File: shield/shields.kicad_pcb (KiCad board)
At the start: 2 copper layers, 40.4 x 95.7 mm, 1 part

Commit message: Update as ordered.
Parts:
- added REF**: C_1210_3225Metric_Pad1.33x2.70mm_HandSolder, Swadge_Parts:C_1210_3225Metric_Pad1.33x2.70mm_HandSolder, F.Cu at (28.7, 116.0)
- added REF**: C_1210_3225Metric_Pad1.33x2.70mm_HandSolder, Swadge_Parts:C_1210_3225Metric_Pad1.33x2.70mm_HandSolder, F.Cu at (23.5, 73.1)
- added REF**: C_1210_3225Metric_Pad1.33x2.70mm_HandSolder, Swadge_Parts:C_1210_3225Metric_Pad1.33x2.70mm_HandSolder, F.Cu at (50.2, 30.3)
- added REF**: C_1210_3225Metric_Pad1.33x2.70mm_HandSolder, Swadge_Parts:C_1210_3225Metric_Pad1.33x2.70mm_HandSolder, F.Cu at (54.9, 94.2)
- added REF**: C_1210_3225Metric_Pad1.33x2.70mm_HandSolder, Swadge_Parts:C_1210_3225Metric_Pad1.33x2.70mm_HandSolder, B.Cu at (55.0, 94.2)
- added REF**: C_1210_3225Metric_Pad1.33x2.70mm_HandSolder, Swadge_Parts:C_1210_3225Metric_Pad1.33x2.70mm_HandSolder, B.Cu at (29.1, 116.9)
- added REF**: C_1210_3225Metric_Pad1.33x2.70mm_HandSolder, Swadge_Parts:C_1210_3225Metric_Pad1.33x2.70mm_HandSolder, B.Cu at (50.2, 30.2)
- added REF**: C_1210_3225Metric_Pad1.33x2.70mm_HandSolder, Swadge_Parts:C_1210_3225Metric_Pad1.33x2.70mm_HandSolder, B.Cu at (23.5, 73.1)
- moved Ref** 114.5 mm to (86.2, 75.3)
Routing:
- net (no net): track 0.00 -> 5.20 mm
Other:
- rule pad_to_mask_clearance: 0.2 -> 0
- board text added: "Fab notes: 0.6mm Thick FR4"
- board text added: "Kidney Test Rev A"

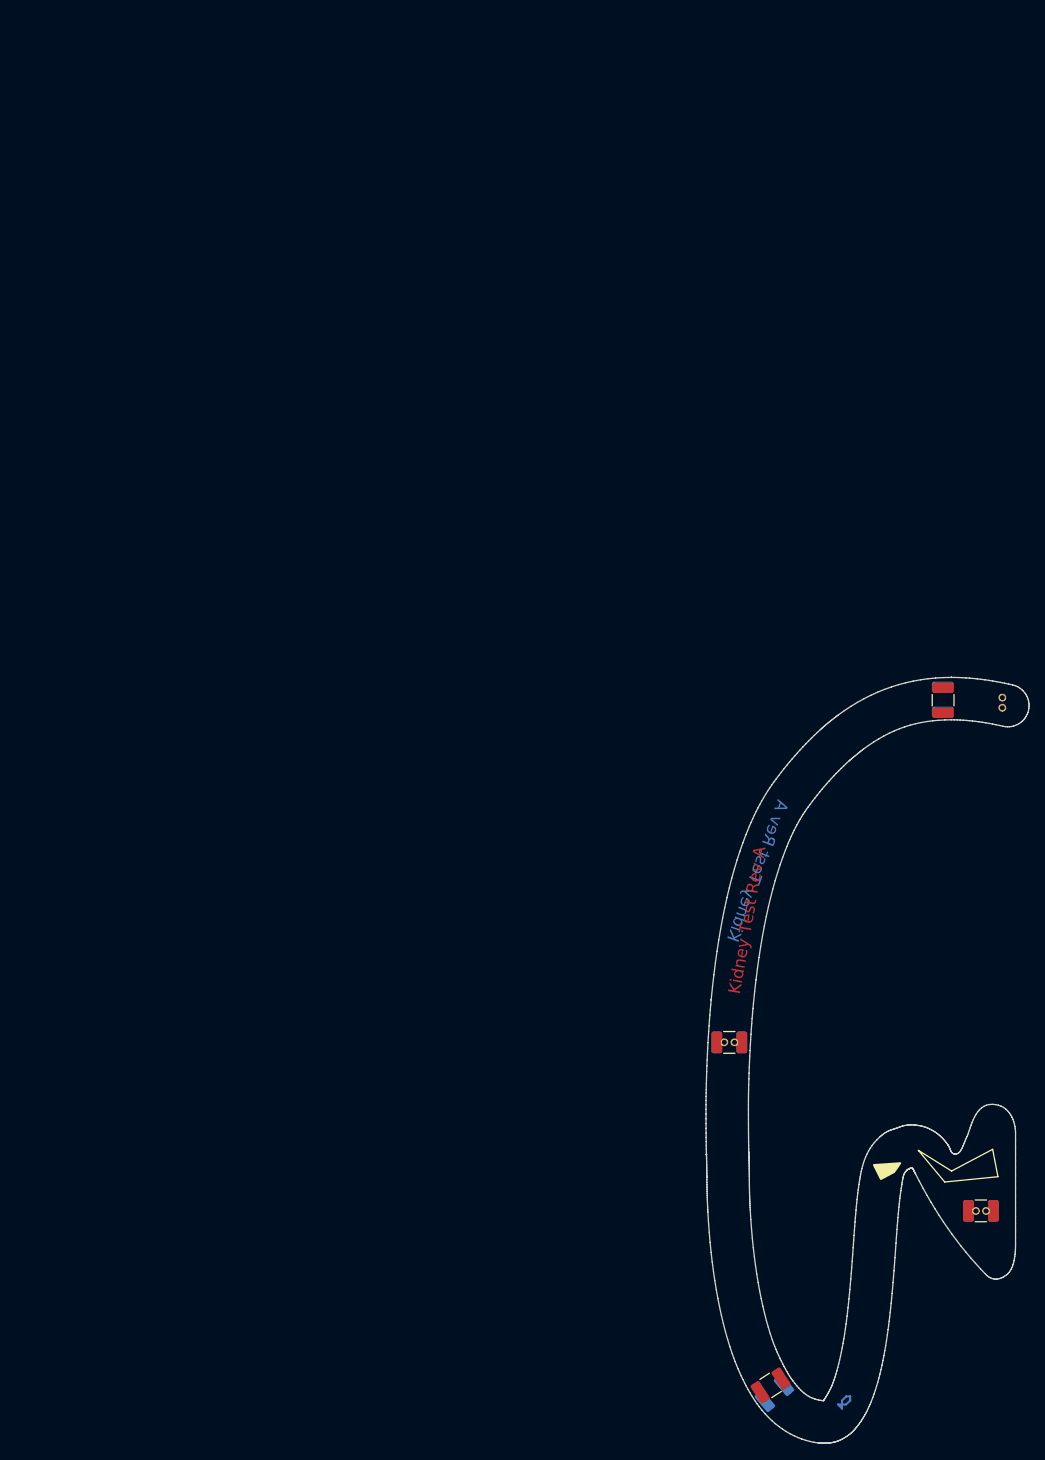
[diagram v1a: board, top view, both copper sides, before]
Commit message: Put squarewave art on shields
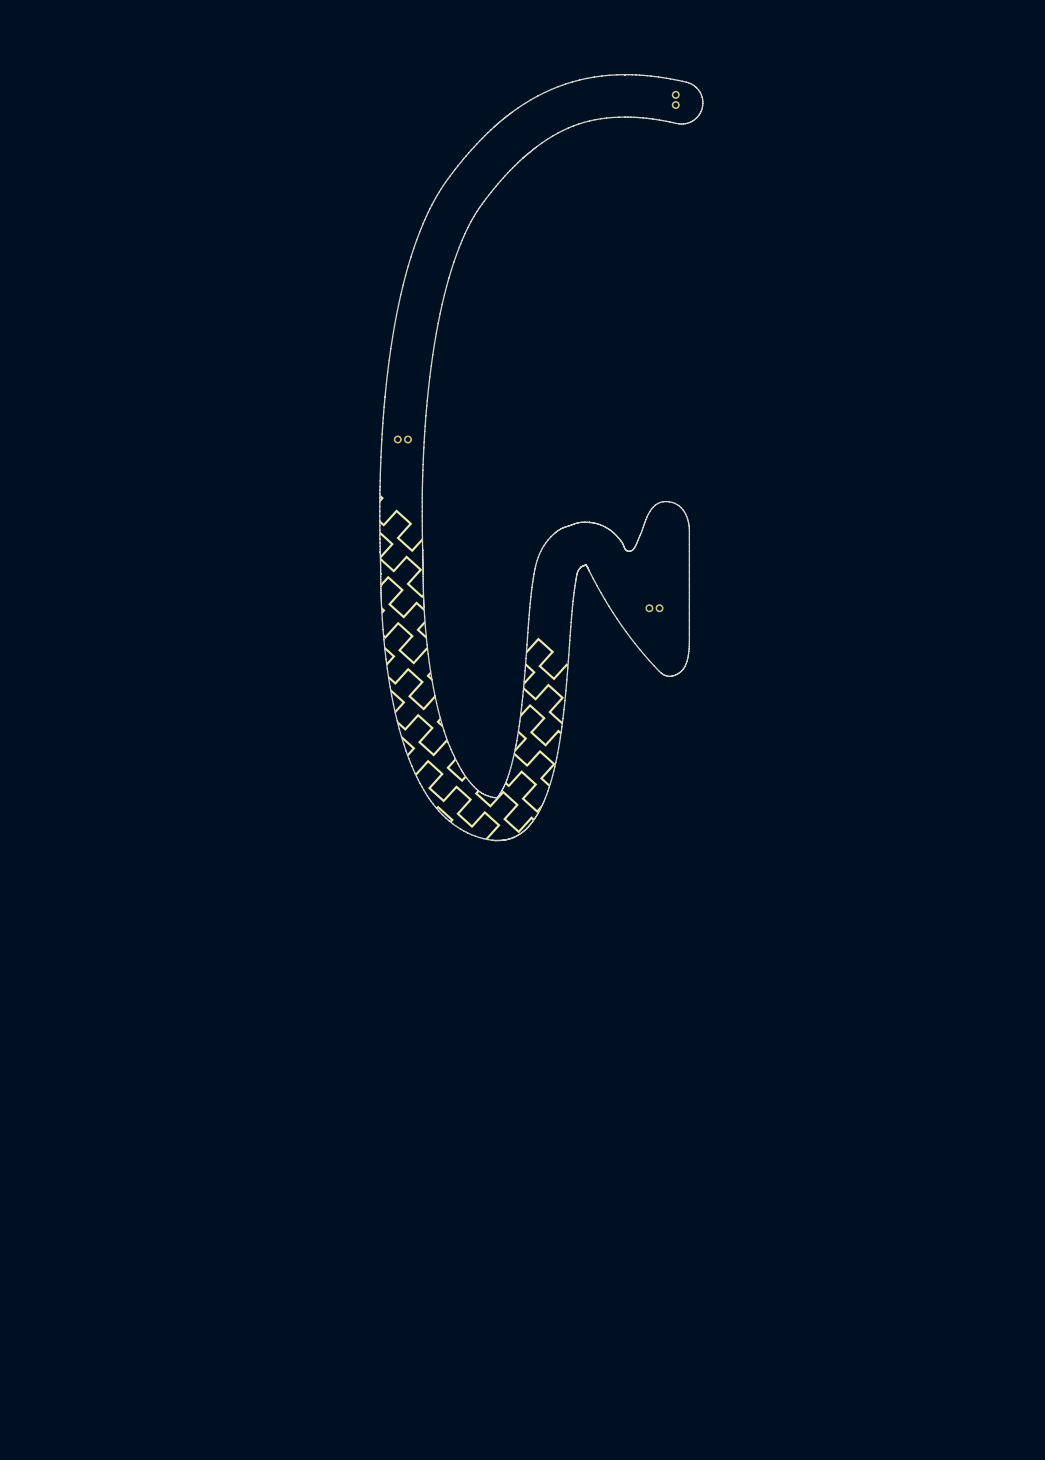
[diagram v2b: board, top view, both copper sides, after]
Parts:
- removed REF** (x8): C_1210_3225Metric_Pad1.33x2.70mm_HandSolder, Swadge_Parts:C_1210_3225Metric_Pad1.33x2.70mm_HandSolder
- added G*** (x7): LOGO, LOGO, F.Cu at (0.00, 0.00)
- moved Ref** 85.7 mm to (45.4, 0.00)
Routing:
- net (no net): track 5.20 -> 0.00 mm
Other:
- outline, holes or cut-outs redrawn
- rule pad_to_mask_clearance: 0 -> 0.2
- board text removed: "Fab notes: 0.6mm Thick FR4"
- board text removed: "Kidney Test Rev A"

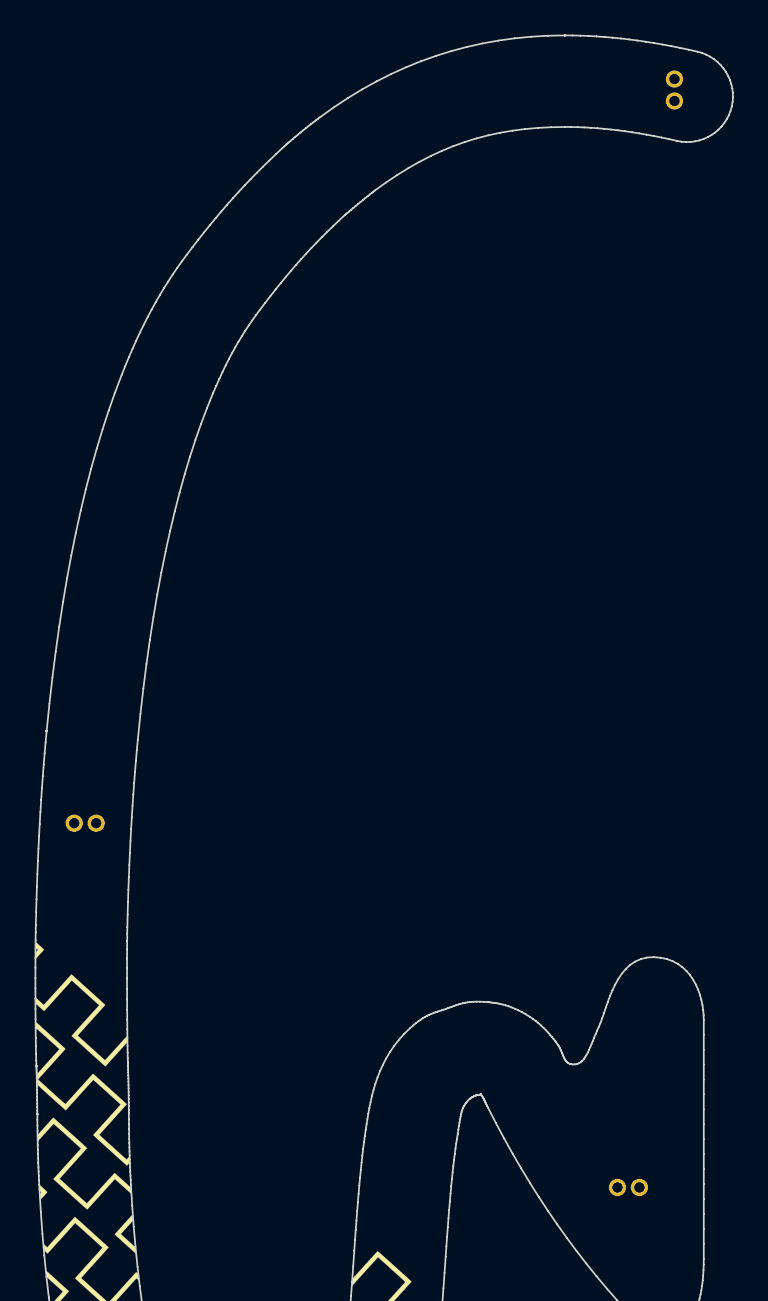
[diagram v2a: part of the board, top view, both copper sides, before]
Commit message: Embiggen holes on shield, remove standoff capacitors, tie all standoff pins to GND
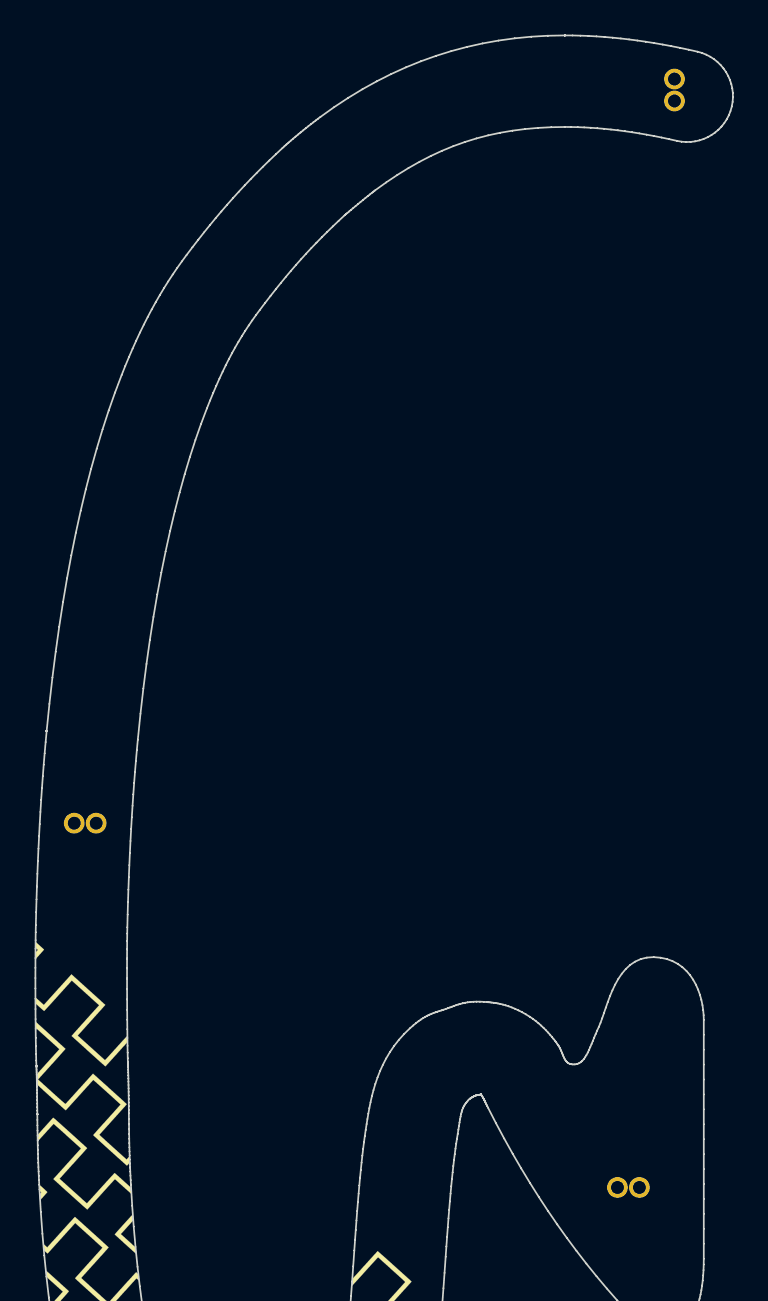
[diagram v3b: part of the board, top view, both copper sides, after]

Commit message: Tweak export for sheilds
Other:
- rule pad_to_mask_clearance: 0.2 -> 0
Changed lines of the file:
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@@
   )
   (setup
-    (pad_to_mask_clearance 0.2)
+    (stackup
+      (layer "F.SilkS" (type "Top Silk Screen"))
+      (layer "F.Paste" (type "Top Solder Paste"))
+      (layer "F.Mask" (type "Top Solder Mask") (thickness 0.01))
+      (layer "F.Cu" (type "copper") (thickness 0.035))
+      (layer "dielectric 1" (type "core") (thickness 1.51) (material "FR4") (epsilon_r 4.5) (loss_tangent 0.02))
+      (layer "B.Cu" (type "copper") (thickness 0.035))
+      (layer "B.Mask" (type "Bottom Solder Mask") (thickness 0.01))
+      (layer "B.Paste" (type "Bottom Solder Paste"))
+      (layer "B.SilkS" (type "Bottom Silk Screen"))
+      (copper_finish "None")
+      (dielectric_constraints no)
+    )
+    (pad_to_mask_clearance 0)
     (pcbplotparams
-      (layerselection 0x00010f0_80000001)
+      (layerselection 0x00010f0_ffffffff)
       (disableapertmacros false)
-      (usegerberextensions false)
+      (usegerberextensions true)
       (usegerberattributes true)
       (usegerberadvancedattributes true)
-      (creategerberjobfile true)
+      (creategerberjobfile false)
       (svguseinch false)
       (svgprecision 6)
@@
       (psnegative false)
       (psa4output false)
-      (plotreference true)
-      (plotvalue true)
+      (plotreference false)
+      (plotvalue false)
       (plotinvisibletext false)
       (sketchpadsonfab false)
@@
       (outputformat 1)
       (mirror false)
-      (drillshape 1)
+      (drillshape 0)
       (scaleselection 1)
       (outputdirectory "gerbers/")

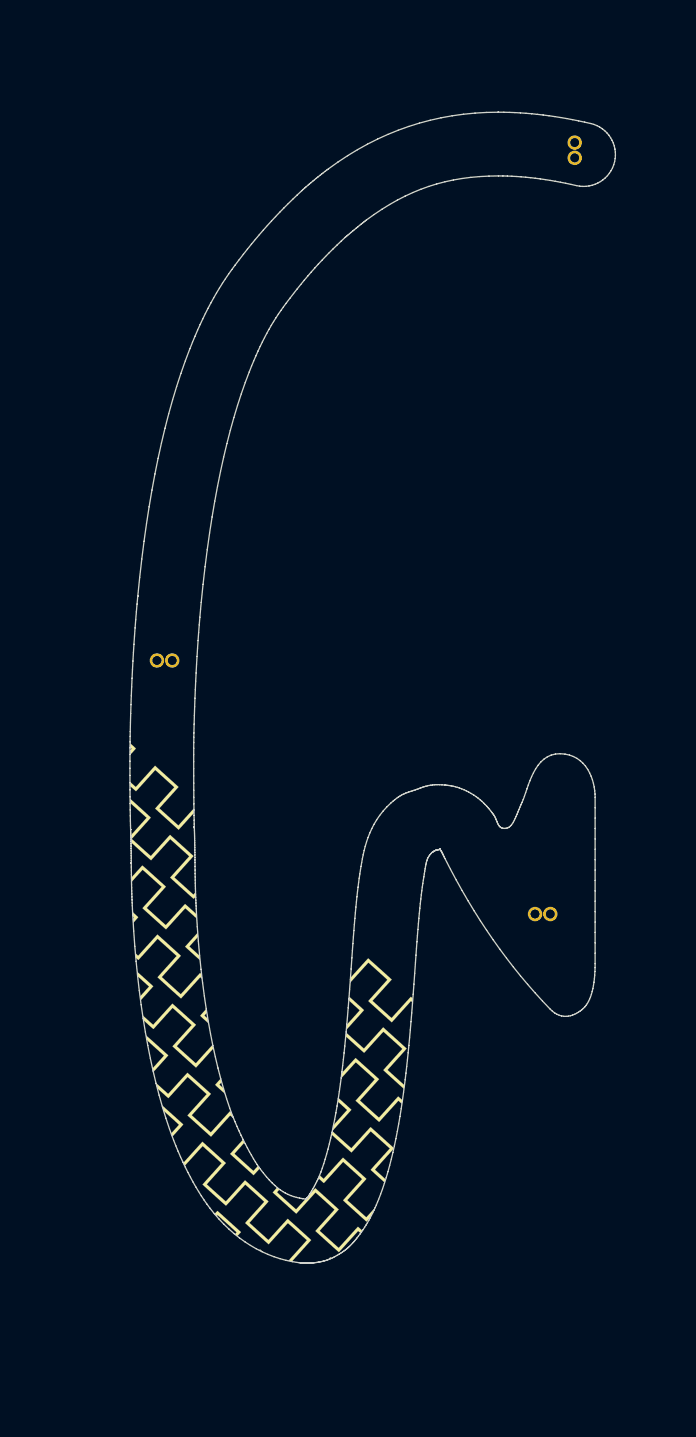
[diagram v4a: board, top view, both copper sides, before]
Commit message: Add metal to sheilds
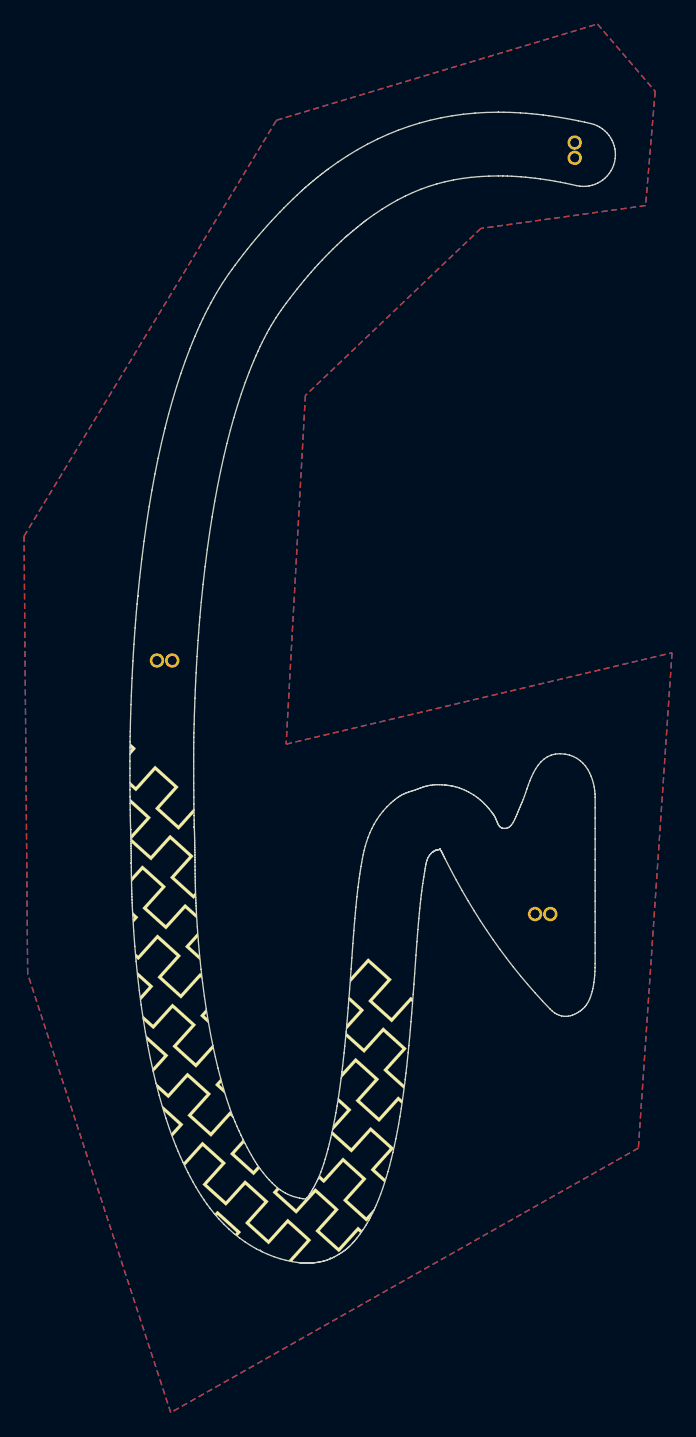
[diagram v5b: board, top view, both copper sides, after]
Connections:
- Ref** pad 1: (no net) -> GND
- Ref** pad 2: (no net) -> GND
- Ref** pad 3: (no net) -> GND
- Ref** pad 4: (no net) -> GND
- Ref** pad 5: (no net) -> GND
- Ref** pad 6: (no net) -> GND
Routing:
- added copper zone on B.Cu, net GND
- added copper zone on F.Cu, net GND
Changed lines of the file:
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@@
   )
   (net 0 "")
+  (net 1 "GND")
   (footprint "LOGO" (layer "F.Cu")
     (at 0 0)
@@
         (xy -30.542392 18.329714)
       ) (layer "Dwgs.User") (width 0.01) (fill solid))
-    (pad "1" thru_hole circle (at -28.58 -45.34) (size 1.2 1.2) (drill 0.75) (layers *.Cu *.Mask))
-    (pad "2" thru_hole circle (at -28.58 -44.07) (size 1.2 1.2) (drill 0.75) (layers *.Cu *.Mask))
-    (pad "3" thru_hole circle (at -63.33 -2.26) (size 1.2 1.2) (drill 0.75) (layers *.Cu *.Mask))
-    (pad "4" thru_hole circle (at -62.06 -2.26) (size 1.2 1.2) (drill 0.75) (layers *.Cu *.Mask))
-    (pad "5" thru_hole circle (at -31.88 18.83) (size 1.2 1.2) (drill 0.75) (layers *.Cu *.Mask))
-    (pad "6" thru_hole circle (at -30.61 18.83) (size 1.2 1.2) (drill 0.75) (layers *.Cu *.Mask))
+    (pad "1" thru_hole circle (at -28.58 -45.34) (size 1.2 1.2) (drill 0.75) (layers *.Cu *.Mask)
+      (net 1 "GND"))
+    (pad "2" thru_hole circle (at -28.58 -44.07) (size 1.2 1.2) (drill 0.75) (layers *.Cu *.Mask)
+      (net 1 "GND"))
+    (pad "3" thru_hole circle (at -63.33 -2.26) (size 1.2 1.2) (drill 0.75) (layers *.Cu *.Mask)
+      (net 1 "GND"))
+    (pad "4" thru_hole circle (at -62.06 -2.26) (size 1.2 1.2) (drill 0.75) (layers *.Cu *.Mask)
+      (net 1 "GND"))
+    (pad "5" thru_hole circle (at -31.88 18.83) (size 1.2 1.2) (drill 0.75) (layers *.Cu *.Mask)
+      (net 1 "GND"))
+    (pad "6" thru_hole circle (at -30.61 18.83) (size 1.2 1.2) (drill 0.75) (layers *.Cu *.Mask)
+      (net 1 "GND"))
   )
   (footprint "LOGO" (layer "F.Cu")
@@
   (gr_line (start -2.150547 27.999059) (end -2.207417 28.635284) (layer "Edge.Cuts") (width 0.1))
   (gr_line (start -5.148034 41.984711) (end -5.216664 42.099721) (layer "Edge.Cuts") (width 0.1))
+  (zone (net 1) (net_name "GND") (layers F&B.Cu) (hatch edge 0.508)
+    (connect_pads (clearance 0))
+    (min_thickness 0.0254) (filled_areas_thickness no)
+    (fill yes (thermal_gap 0.05) (thermal_bridge_width 0.5))
+    (polygon
+      (pts
+        (xy 23.5 -49.6)
+        (xy 22.7 -40.1)
+        (xy 9 -38.2)
+        (xy -5.6 -24.3)
+        (xy -7.2 4.7)
+        (xy 24.9 -2.9)
+        (xy 22.1 38.3)
+        (xy -16.8 60.3)
+        (xy -28.7 23.8)
+        (xy -29 -12.6)
+        (xy -8 -47.2)
+        (xy 18.7 -55.2)
+      )
+    )
+  )
 )
